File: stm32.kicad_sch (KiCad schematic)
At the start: 15 parts, among them J1 TC2030-IDC, J7 Conn_01x03, U2 STM32F410CBU6

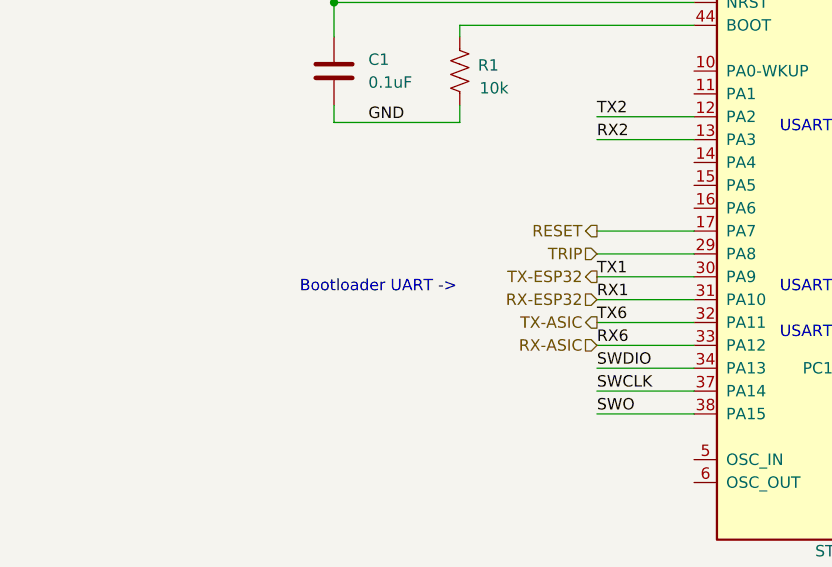
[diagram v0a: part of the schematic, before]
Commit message: added test points for #7
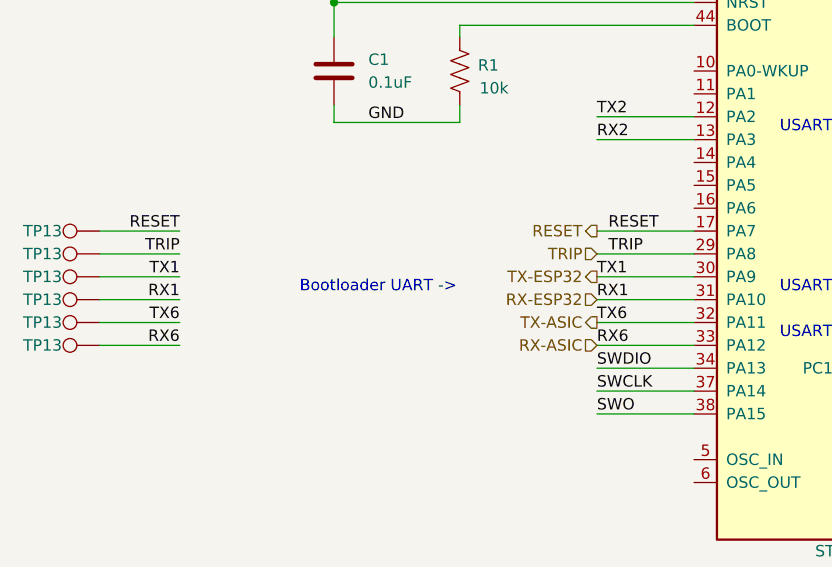
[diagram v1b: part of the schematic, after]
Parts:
- added TP13 (x6): TestPoint, TestPoint:TestPoint_Pad_D1.0mm, symbol Connector:TestPoint
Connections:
- net RESET: now also TP13.1
- net RX-ASIC: now also TP13.1
- net RX-ESP32: now also TP13.1
- net TRIP: now also TP13.1
- net TX-ASIC: now also TP13.1
- net TX-ESP32: now also TP13.1

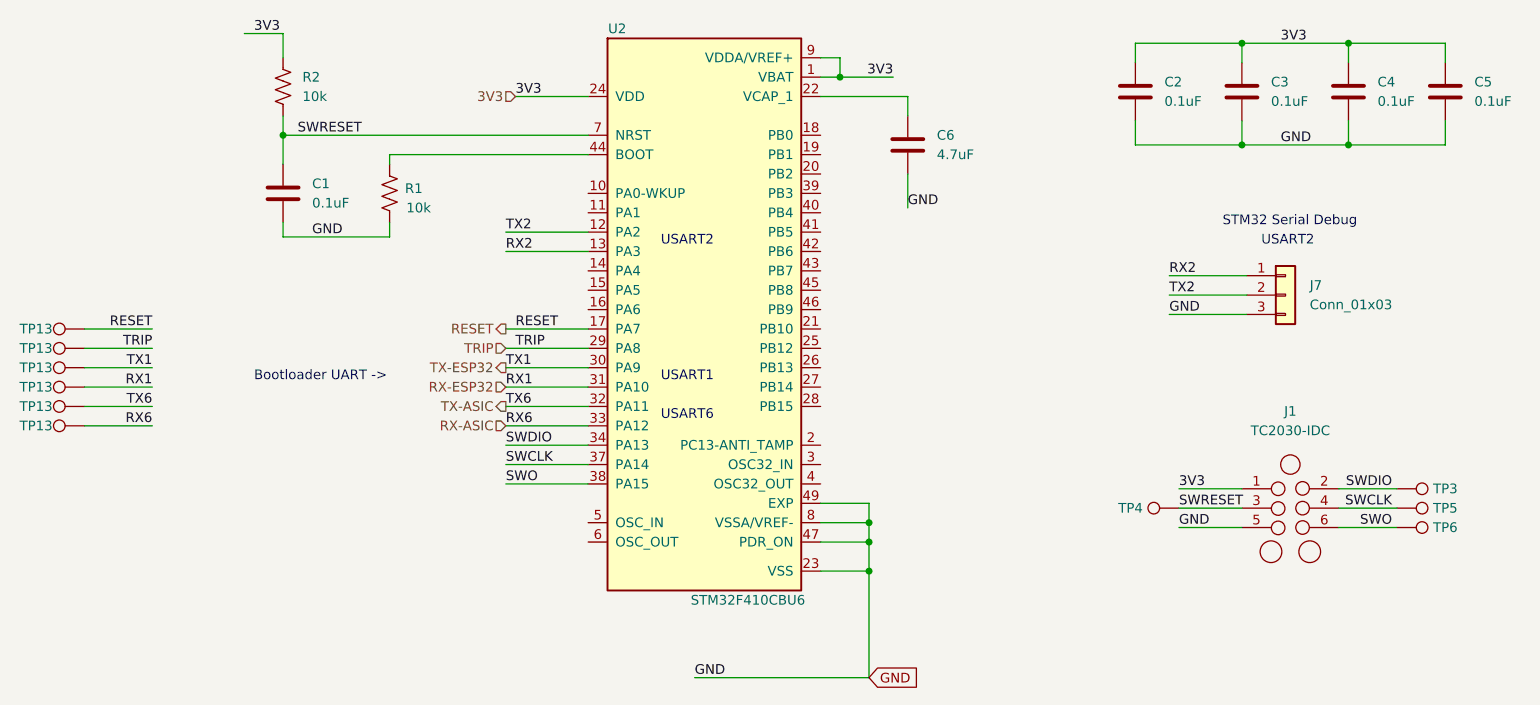
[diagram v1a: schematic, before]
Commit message: changed buttons for #5 flipped display for #2
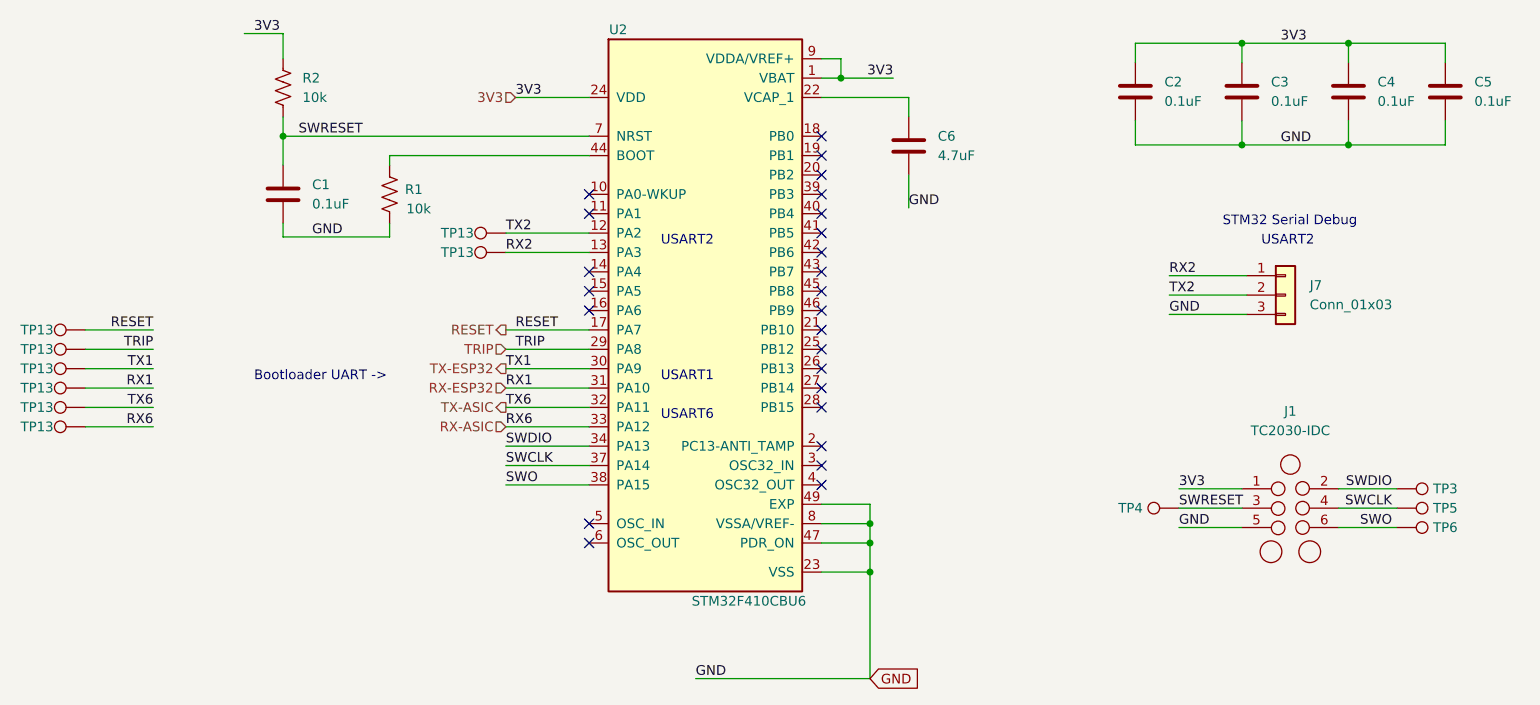
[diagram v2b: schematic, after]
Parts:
- added TP13 (x2): TestPoint, TestPoint:TestPoint_Pad_D1.0mm, symbol Connector:TestPoint
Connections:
- net RX2: now also TP13.1
- net TX2: now also TP13.1
- no-connect marks 0 -> 25

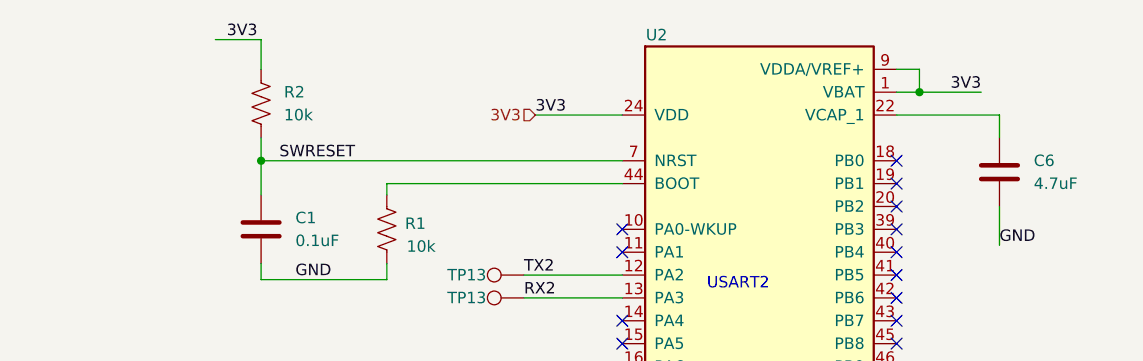
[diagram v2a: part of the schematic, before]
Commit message: switched barrel plug for #8. touched up schematic, DRC, generated BOM, generated Gerbers
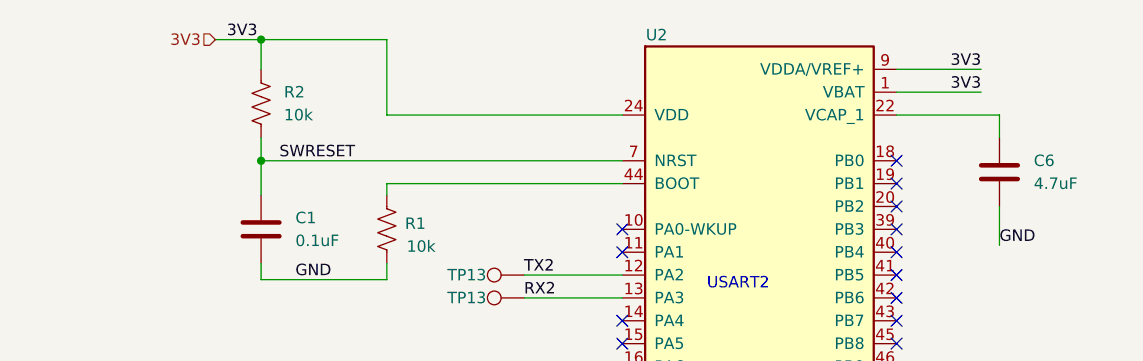
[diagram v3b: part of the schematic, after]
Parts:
- J1, J7: now left out of the parts list
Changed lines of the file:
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@@
   (title_block
     (title "blockaxe1")
-    (date "2023-11-15")
-    (rev "1")
+    (date "2024-02-21")
+    (rev "2")
   )
   (junction (at 140.462 118.872) (diameter 0) (color 0 0 0 0)
@@
   (junction (at 140.462 121.412) (diameter 0) (color 0 0 0 0)
   )
+  (junction (at 63.5 54.61) (diameter 0) (color 0 0 0 0)
+  )
   (junction (at 203.2 55.88) (diameter 0) (color 0 0 0 0)
-  )
-  (junction (at 136.652 60.452) (diameter 0) (color 0 0 0 0)
   )
   (junction (at 203.2 69.215) (diameter 0) (color 0 0 0 0)
@@
     (stroke (width 0) (type default))
   )
+  (wire (pts (xy 77.47 62.992) (xy 77.47 54.61))
+    (stroke (width 0) (type default))
+  )
   (wire (pts (xy 63.5 79.502) (xy 63.5 81.28))
     (stroke (width 0) (type default))
@@
     (stroke (width 0) (type default))
   )
-  (wire (pts (xy 93.98 62.992) (xy 103.632 62.992))
-    (stroke (width 0) (type default))
-  )
   (wire (pts (xy 58.42 54.61) (xy 63.5 54.61))
     (stroke (width 0) (type default))
@@
     (stroke (width 0) (type default))
   )
+  (wire (pts (xy 134.112 60.452) (xy 143.51 60.452))
+    (stroke (width 0) (type default))
+  )
   (wire (pts (xy 134.112 125.222) (xy 140.462 125.222))
     (stroke (width 0) (type default))
@@
     (stroke (width 0) (type default))
   )
-  (wire (pts (xy 134.112 60.452) (xy 136.652 60.452))
-    (stroke (width 0) (type default))
-  )
   (wire (pts (xy 103.632 70.612) (xy 77.47 70.612))
     (stroke (width 0) (type default))
@@
     (stroke (width 0) (type default))
   )
-  (wire (pts (xy 134.112 57.912) (xy 136.652 57.912))
-    (stroke (width 0) (type default))
-  )
-  (wire (pts (xy 136.652 60.452) (xy 143.51 60.452))
+  (wire (pts (xy 134.112 57.912) (xy 143.51 57.912))
     (stroke (width 0) (type default))
   )
@@
     (stroke (width 0) (type default))
   )
+  (wire (pts (xy 103.632 62.992) (xy 77.47 62.992))
+    (stroke (width 0) (type default))
+  )
   (wire (pts (xy 117.602 139.192) (xy 140.462 139.192))
     (stroke (width 0) (type default))
   )
+  (wire (pts (xy 77.47 54.61) (xy 63.5 54.61))
+    (stroke (width 0) (type default))
+  )
   (wire (pts (xy 92.71 111.252) (xy 103.632 111.252))
     (stroke (width 0) (type default))
@@
     (stroke (width 0) (type default))
   )
-  (wire (pts (xy 136.652 57.912) (xy 136.652 60.452))
-    (stroke (width 0) (type default))
-  )
   (wire (pts (xy 92.71 113.792) (xy 103.632 113.792))
     (stroke (width 0) (type default))
@@
     (effects (font (size 1.27 1.27)) (justify left bottom))
   )
-  (label "3V3" (at 93.98 62.992 0) (fields_autoplaced)
-    (effects (font (size 1.27 1.27)) (justify left bottom))
-  )
   (label "GND" (at 145.542 77.47 0) (fields_autoplaced)
     (effects (font (size 1.27 1.27)) (justify left bottom))
@@
     (effects (font (size 1.27 1.27)) (justify right bottom))
   )
+  (label "3V3" (at 143.51 60.452 180) (fields_autoplaced)
+    (effects (font (size 1.27 1.27)) (justify right bottom))
+  )
   (label "SWDIO" (at 208.915 114.3 180) (fields_autoplaced)
     (effects (font (size 1.27 1.27)) (justify right bottom))
@@
     (effects (font (size 1.27 1.27)) (justify left bottom))
   )
-  (label "3V3" (at 143.51 60.452 180) (fields_autoplaced)
+  (label "3V3" (at 143.51 57.912 180) (fields_autoplaced)
     (effects (font (size 1.27 1.27)) (justify right bottom))
   )
@@
     (effects (font (size 1.27 1.27)) (justify right))
   )
-  (hierarchical_label "3V3" (shape input) (at 93.98 62.992 180) (fields_autoplaced)
+  (hierarchical_label "3V3" (shape input) (at 58.42 54.61 180) (fields_autoplaced)
     (effects (font (size 1.27 1.27)) (justify right))
   )
@@
   )
   (symbol (lib_id "Connector_Generic:Conn_01x03") (at 194.945 88.9 0) (unit 1)
-    (in_bom yes) (on_board yes) (dnp no) (fields_autoplaced)
+    (in_bom no) (on_board yes) (dnp no) (fields_autoplaced)
     (property "Reference" "J7" (at 198.12 87.63 0)
       (effects (font (size 1.27 1.27)) (justify left))
@@
   )
   (symbol (lib_id "blockaxe:TC2030-IDC-NL") (at 195.58 116.84 0) (unit 1)
-    (in_bom yes) (on_board yes) (dnp no) (fields_autoplaced)
+    (in_bom no) (on_board yes) (dnp no) (fields_autoplaced)
     (property "Reference" "J1" (at 195.58 104.14 0)
       (effects (font (size 1.27 1.27)))

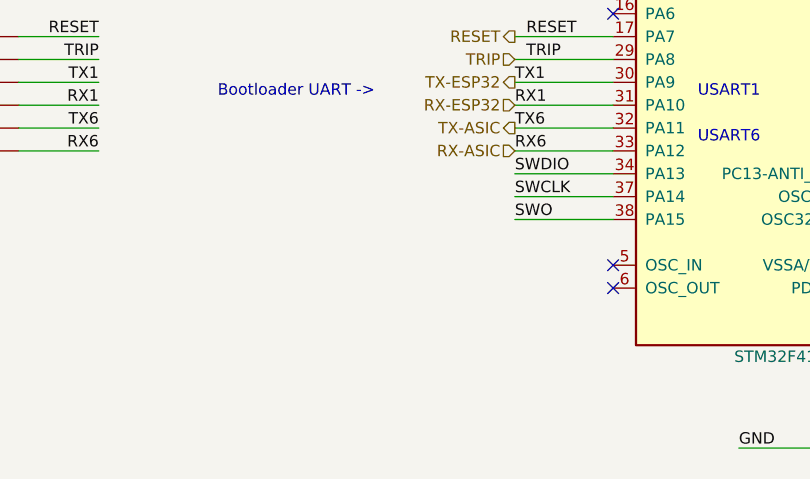
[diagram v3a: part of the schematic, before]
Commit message: added stm32 crystal for #9
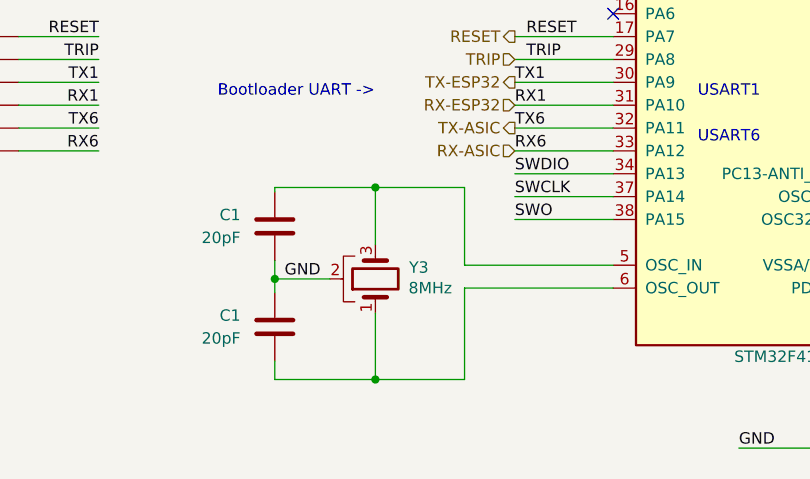
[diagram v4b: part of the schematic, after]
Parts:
- added C1 (x2): 20pF, Capacitor_SMD:C_0402_1005Metric, symbol Device:C
- added Y3: 8MHz, blockaxe:XTAL_ECS-240-8-33-AGN-TR, symbol Device:Crystal_GND24-combined_GND
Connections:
- net GND: now also C1.1, C1.2, Y3.2, Y3.4
- net at U2.5 (OSC_IN): now also C1.1, Y3.3
- net at U2.6 (OSC_OUT): now also C1.2, Y3.1
- no-connect marks 25 -> 23
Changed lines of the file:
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@@
   (junction (at 63.5 68.072) (diameter 0) (color 0 0 0 0)
   )
+  (junction (at 77.216 131.572) (diameter 0) (color 0 0 0 0)
+  )
   (junction (at 189.23 55.88) (diameter 0) (color 0 0 0 0)
   )
@@
   )
   (junction (at 140.462 125.222) (diameter 0) (color 0 0 0 0)
+  )
+  (junction (at 77.216 110.236) (diameter 0) (color 0 0 0 0)
+  )
+  (junction (at 66.04 120.396) (diameter 0) (color 0 0 0 0)
   )
   (junction (at 140.462 121.412) (diameter 0) (color 0 0 0 0)
@@
   (no_connect (at 134.112 80.772))
   (no_connect (at 134.112 78.232))
-  (no_connect (at 103.632 121.412))
   (no_connect (at 134.112 96.012))
   (no_connect (at 134.112 85.852))
@@
   (no_connect (at 134.112 108.712))
   (no_connect (at 134.112 90.932))
-  (no_connect (at 103.632 118.872))
   (no_connect (at 134.112 101.092))
   (no_connect (at 134.112 70.612))
@@
     (stroke (width 0) (type default))
   )
+  (wire (pts (xy 77.216 131.572) (xy 87.122 131.572))
+    (stroke (width 0) (type default))
+  )
+  (wire (pts (xy 66.04 120.396) (xy 66.04 121.92))
+    (stroke (width 0) (type default))
+  )
   (wire (pts (xy 63.5 68.072) (xy 63.5 71.882))
     (stroke (width 0) (type default))
@@
     (stroke (width 0) (type default))
   )
+  (wire (pts (xy 87.122 131.572) (xy 87.122 121.412))
+    (stroke (width 0) (type default))
+  )
   (wire (pts (xy 179.705 91.44) (xy 189.865 91.44))
     (stroke (width 0) (type default))
@@
     (stroke (width 0) (type default))
   )
+  (wire (pts (xy 66.04 131.572) (xy 77.216 131.572))
+    (stroke (width 0) (type default))
+  )
   (wire (pts (xy 63.5 54.61) (xy 63.5 57.912))
     (stroke (width 0) (type default))
@@
     (stroke (width 0) (type default))
   )
+  (wire (pts (xy 72.136 120.396) (xy 66.04 120.396))
+    (stroke (width 0) (type default))
+  )
   (wire (pts (xy 145.542 73.152) (xy 145.542 77.47))
     (stroke (width 0) (type default))
@@
     (stroke (width 0) (type default))
   )
+  (wire (pts (xy 66.04 120.396) (xy 66.04 118.364))
+    (stroke (width 0) (type default))
+  )
   (wire (pts (xy 203.2 69.215) (xy 189.23 69.215))
     (stroke (width 0) (type default))
@@
     (stroke (width 0) (type default))
   )
+  (wire (pts (xy 103.632 118.872) (xy 87.122 118.872))
+    (stroke (width 0) (type default))
+  )
   (wire (pts (xy 77.47 79.502) (xy 77.47 81.28))
     (stroke (width 0) (type default))
@@
     (stroke (width 0) (type default))
   )
+  (wire (pts (xy 77.216 110.236) (xy 87.122 110.236))
+    (stroke (width 0) (type default))
+  )
+  (wire (pts (xy 66.04 110.236) (xy 77.216 110.236))
+    (stroke (width 0) (type default))
+  )
   (wire (pts (xy 63.5 81.28) (xy 77.47 81.28))
     (stroke (width 0) (type default))
@@
     (stroke (width 0) (type default))
   )
+  (wire (pts (xy 77.216 110.236) (xy 77.216 116.586))
+    (stroke (width 0) (type default))
+  )
   (wire (pts (xy 134.112 62.992) (xy 145.542 62.992))
     (stroke (width 0) (type default))
@@
     (stroke (width 0) (type default))
   )
+  (wire (pts (xy 66.04 129.54) (xy 66.04 131.572))
+    (stroke (width 0) (type default))
+  )
   (wire (pts (xy 37.592 106.172) (xy 46.482 106.172))
     (stroke (width 0) (type default))
@@
     (stroke (width 0) (type default))
   )
+  (wire (pts (xy 87.122 118.872) (xy 87.122 110.236))
+    (stroke (width 0) (type default))
+  )
   (wire (pts (xy 92.71 111.252) (xy 103.632 111.252))
     (stroke (width 0) (type default))
@@
     (stroke (width 0) (type default))
   )
+  (wire (pts (xy 77.216 124.206) (xy 77.216 131.572))
+    (stroke (width 0) (type default))
+  )
+  (wire (pts (xy 66.04 110.744) (xy 66.04 110.236))
+    (stroke (width 0) (type default))
+  )
   (wire (pts (xy 92.71 113.792) (xy 103.632 113.792))
     (stroke (width 0) (type default))
@@
   )
   (wire (pts (xy 203.2 55.88) (xy 189.23 55.88))
+    (stroke (width 0) (type default))
+  )
+  (wire (pts (xy 87.122 121.412) (xy 103.632 121.412))
     (stroke (width 0) (type default))
   )
@@
   (label "SWRESET" (at 180.975 116.84 0) (fields_autoplaced)
     (effects (font (size 1.27 1.27)) (justify left bottom))
+  )
+  (label "GND" (at 71.12 120.396 180) (fields_autoplaced)
+    (effects (font (size 1.27 1.27)) (justify right bottom))
   )
   (label "GND" (at 180.975 119.38 0) (fields_autoplaced)
@@
     )
   )
+  (symbol (lib_id "Device:C") (at 66.04 114.554 0) (mirror y) (unit 1)
+    (in_bom yes) (on_board yes) (dnp no)
+    (property "Reference" "C1" (at 62.23 113.284 0)
+      (effects (font (size 1.27 1.27)) (justify left))
+    )
+    (property "Value" "20pF" (at 62.23 115.824 0)
+      (effects (font (size 1.27 1.27)) (justify left))
+    )
+    (property "Footprint" "Capacitor_SMD:C_0402_1005Metric" (at 65.0748 118.364 0)
+      (effects (font (size 1.27 1.27)) hide)
+    )
+    (property "Datasheet" "~" (at 66.04 114.554 0)
+      (effects (font (size 1.27 1.27)) hide)
+    )
+    (property "DK" "490-GCM1555C1H200JA16DCT-ND" (at 66.04 114.554 0)
+      (effects (font (size 1.27 1.27)) hide)
+    )
+    (property "PARTNO" "GCM1555C1H200JA16D" (at 66.04 114.554 0)
+      (effects (font (size 1.27 1.27)) hide)
+    )
+    (pin "1")
+    (pin "2")
+    (instances
+      (project "blockaxe1"
+        (path "/a166cb37-4e3a-4be5-b2da-277a3281a4de"
+          (reference "C1") (unit 1)
+        )
+        (path "/a166cb37-4e3a-4be5-b2da-277a3281a4de/a2f53eaa-4b17-468c-8132-e21e20b70349"
+          (reference "C8") (unit 1)
+        )
+      )
+    )
+  )
+  (symbol (lib_id "Device:C") (at 66.04 125.73 0) (mirror y) (unit 1)
+    (in_bom yes) (on_board yes) (dnp no)
+    (property "Reference" "C1" (at 62.23 124.46 0)
+      (effects (font (size 1.27 1.27)) (justify left))
+    )
+    (property "Value" "20pF" (at 62.23 127 0)
+      (effects (font (size 1.27 1.27)) (justify left))
+    )
+    (property "Footprint" "Capacitor_SMD:C_0402_1005Metric" (at 65.0748 129.54 0)
+      (effects (font (size 1.27 1.27)) hide)
+    )
+    (property "Datasheet" "~" (at 66.04 125.73 0)
+      (effects (font (size 1.27 1.27)) hide)
+    )
+    (property "DK" "490-GCM1555C1H200JA16DCT-ND" (at 66.04 125.73 0)
+      (effects (font (size 1.27 1.27)) hide)
+    )
+    (property "PARTNO" "GCM1555C1H200JA16D" (at 66.04 125.73 0)
+      (effects (font (size 1.27 1.27)) hide)
+    )
+    (pin "1")
+    (pin "2")
+    (instances
+      (project "blockaxe1"
+        (path "/a166cb37-4e3a-4be5-b2da-277a3281a4de"
+          (reference "C1") (unit 1)
+        )
+        (path "/a166cb37-4e3a-4be5-b2da-277a3281a4de/a2f53eaa-4b17-468c-8132-e21e20b70349"
+          (reference "C9") (unit 1)
+        )
+      )
+    )
+  )
   (symbol (lib_id "Device:C") (at 215.9 62.23 0) (unit 1)
     (in_bom yes) (on_board yes) (dnp no) (fields_autoplaced)
@@
         )
       )
+    )
+  )
+  (symbol (lib_id "Device:Crystal_GND24-combined_GND") (at 77.216 120.396 90) (unit 1)
+    (in_bom yes) (on_board yes) (dnp no)
+    (property "Reference" "Y3" (at 82.042 119.126 90)
+      (effects (font (size 1.27 1.27)))
+    )
+    (property "Value" "8MHz" (at 83.312 121.412 90)
+      (effects (font (size 1.27 1.27)))
+    )
+    (property "Footprint" "blockaxe:XTAL_ECS-240-8-33-AGN-TR" (at 77.216 120.396 0)
+      (effects (font (size 1.27 1.27)) hide)
+    )
+    (property "Datasheet" "~" (at 77.216 120.396 0)
+      (effects (font (size 1.27 1.27)) hide)
+    )
+    (property "DK" "50-ECS-80-12-33-JGN-CT-ND" (at 77.216 120.396 0)
+      (effects (font (size 1.27 1.27)) hide)
+    )
+    (property "PARTNO" "ECS-80-12-33-JGN-TR" (at 77.216 120.396 0)
+      (effects (font (size 1.27 1.27)) hide)
+    )
+    (pin "1")
+    (pin "3")
+    (pin "4")
+    (pin "2")
+    (instances
+      (project "blockaxe1"
+        (path "/a166cb37-4e3a-4be5-b2da-277a3281a4de/a2f53eaa-4b17-468c-8132-e21e20b70349"
+          (reference "Y3") (unit 1)
+        )
+      )
